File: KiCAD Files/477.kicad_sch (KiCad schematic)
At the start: 28 parts, among them J1 USB_A, U1 STM32H7A3RGTx, U2 LM1117DT-3.3, U3 AT25SF081-SSHD-X, U4 AT25SF081-SSHD-X, U5 AT25SF081-SSHD-X, U6 AT25SF081-SSHD-X, Y1 Crystal

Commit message: checking kicad files
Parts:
- C1: value C -> 10u; symbol Device:C -> CustomSymbols:C
- C2: value C -> 22u; symbol Device:C -> CustomSymbols:C
- C3, C4, C5: symbol Device:C -> CustomSymbols:C
- DS1: symbol Display_Character:WC1602A -> CustomSymbols:WC1602A
- J1: symbol Connector:USB_A -> CustomSymbols:USB_A
- R1, R11, R12, R2, R3, R4, R5, R6, R7, R8, R9: symbol Device:R_US -> CustomSymbols:R_US
- R10: value R_US -> 1k; symbol Device:R_US -> CustomSymbols:R_US
- U1: symbol MCU_ST_STM32H7:STM32H7A3RGTx -> CustomSymbols:STM32H7A3RGTx
- U2: value LM1117DT-3.3 -> AZ1117IH-3.3TRG1; symbol Regulator_Linear:LM1117DT-3.3 -> CustomSymbols:LM1117DT-3.3
- U3, U4, U5, U6: value AT25SF081-SSHD-X -> MT29F4G01ABAFDWB-IT:F; symbol Memory_Flash:AT25SF081-SSHD-X -> CustomSymbols:AT25SF081-SSHD-X
- Y1: symbol Device:Crystal -> CustomSymbols:Crystal
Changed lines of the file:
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@@
 	)
 	(symbol
-		(lib_id "power:GND")
+		(lib_id "CustomSymbols:GND")
 		(at 142.24 87.63 0)
 		(unit 1)
@@
 	)
 	(symbol
-		(lib_id "Device:C")
+		(lib_id "CustomSymbols:C")
 		(at 142.24 83.82 0)
 		(unit 1)
@@
 	)
 	(symbol
-		(lib_id "Device:C")
+		(lib_id "CustomSymbols:C")
 		(at 140.97 34.29 0)
 		(unit 1)
@@
 			)
 		)
-		(property "Value" "C"
+		(property "Value" "10u"
 			(at 144.78 35.5599 0)
 			(effects
@@
 	)
 	(symbol
-		(lib_id "Device:C")
+		(lib_id "CustomSymbols:C")
 		(at 172.72 34.29 0)
 		(unit 1)
@@
 			)
 		)
-		(property "Value" "C"
+		(property "Value" "22u"
 			(at 176.53 35.5599 0)
 			(effects
@@
 	)
 	(symbol
-		(lib_id "Device:R_US")
+		(lib_id "CustomSymbols:R_US")
 		(at 207.01 82.55 0)
 		(unit 1)
@@
 	)
 	(symbol
-		(lib_id "power:GND")
+		(lib_id "CustomSymbols:GND")
 		(at 146.05 132.08 0)
 		(unit 1)
@@
 	)
 	(symbol
-		(lib_id "Memory_Flash:AT25SF081-SSHD-X")
+		(lib_id "CustomSymbols:AT25SF081-SSHD-X")
 		(at 212.09 119.38 0)
 		(unit 1)
@@
 			)
 		)
-		(property "Value" "AT25SF081-SSHD-X"
-			(at 189.738 132.08 0)
+		(property "Value" "MT29F4G01ABAFDWB-IT:F"
+			(at 185.42 132.842 0)
 			(effects
 				(font
@@
 	)
 	(symbol
-		(lib_id "power:+3.3V")
+		(lib_id "CustomSymbols:+3.3V")
 		(at 39.37 149.86 0)
 		(unit 1)
@@
 	)
 	(symbol
-		(lib_id "power:GND")
+		(lib_id "CustomSymbols:GND")
 		(at 54.61 121.92 0)
 		(unit 1)
@@
 	)
 	(symbol
-		(lib_id "power:GND")
+		(lib_id "CustomSymbols:GND")
 		(at 250.19 82.55 0)
 		(unit 1)
@@
 	)
 	(symbol
-		(lib_id "Device:R_US")
+		(lib_id "CustomSymbols:R_US")
 		(at 149.86 83.82 0)
 		(unit 1)
@@
 	)
 	(symbol
-		(lib_id "Display_Character:WC1602A")
+		(lib_id "CustomSymbols:WC1602A")
 		(at 39.37 170.18 0)
 		(unit 1)
@@
 	)
 	(symbol
-		(lib_id "Device:R_US")
+		(lib_id "CustomSymbols:R_US")
 		(at 201.93 82.55 0)
 		(unit 1)
@@
 	)
 	(symbol
-		(lib_id "Regulator_Linear:LM1117DT-3.3")
+		(lib_id "CustomSymbols:LM1117DT-3.3")
 		(at 156.21 30.48 0)
 		(unit 1)
@@
 			)
 		)
-		(property "Value" "LM1117DT-3.3"
+		(property "Value" "AZ1117IH-3.3TRG1"
 			(at 156.21 26.67 0)
 			(effects
@@
 	)
 	(symbol
-		(lib_id "Device:Crystal")
+		(lib_id "CustomSymbols:Crystal")
 		(at 209.55 27.94 90)
 		(unit 1)
@@
 	)
 	(symbol
-		(lib_id "Device:R_US")
+		(lib_id "CustomSymbols:R_US")
 		(at 58.42 151.13 0)
 		(unit 1)
@@
 	)
 	(symbol
-		(lib_id "power:+3.3V")
+		(lib_id "CustomSymbols:+3.3V")
 		(at 146.05 106.68 0)
 		(unit 1)
@@
 	)
 	(symbol
-		(lib_id "Device:R_US")
+		(lib_id "CustomSymbols:R_US")
 		(at 58.42 158.75 0)
 		(unit 1)
@@
 	)
 	(symbol
-		(lib_id "MCU_ST_STM32H7:STM32H7A3RGTx")
+		(lib_id "CustomSymbols:STM32H7A3RGTx")
 		(at 54.61 76.2 0)
 		(unit 1)
@@
 	)
 	(symbol
-		(lib_id "power:GND")
+		(lib_id "CustomSymbols:GND")
 		(at 180.34 132.08 0)
 		(unit 1)
@@
 	)
 	(symbol
-		(lib_id "Memory_Flash:AT25SF081-SSHD-X")
+		(lib_id "CustomSymbols:AT25SF081-SSHD-X")
 		(at 243.84 119.38 0)
 		(unit 1)
@@
 			)
 		)
-		(property "Value" "AT25SF081-SSHD-X"
-			(at 221.488 132.08 0)
+		(property "Value" "MT29F4G01ABAFDWB-IT:F"
+			(at 216.408 132.08 0)
 			(effects
 				(font
@@
 	)
 	(symbol
-		(lib_id "Device:R_US")
+		(lib_id "CustomSymbols:R_US")
 		(at 209.55 82.55 0)
 		(unit 1)
@@
 	)
 	(symbol
-		(lib_id "power:+3.3V")
+		(lib_id "CustomSymbols:+3.3V")
 		(at 58.42 147.32 0)
 		(unit 1)
@@
 	)
 	(symbol
-		(lib_id "Device:R_US")
+		(lib_id "CustomSymbols:R_US")
 		(at 214.63 82.55 0)
 		(unit 1)
@@
 	)
 	(symbol
-		(lib_id "power:GND")
+		(lib_id "CustomSymbols:GND")
 		(at 199.39 41.91 0)
 		(unit 1)
@@
 	)
 	(symbol
-		(lib_id "power:GND")
+		(lib_id "CustomSymbols:GND")
 		(at 160.02 80.01 0)
 		(unit 1)
@@
 	)
 	(symbol
-		(lib_id "power:GND")
+		(lib_id "CustomSymbols:GND")
 		(at 243.84 132.08 0)
 		(unit 1)
@@
 	)
 	(symbol
-		(lib_id "Device:R_US")
+		(lib_id "CustomSymbols:R_US")
 		(at 204.47 82.55 0)
 		(unit 1)
@@
 	)
 	(symbol
-		(lib_id "power:+3.3V")
+		(lib_id "CustomSymbols:+3.3V")
 		(at 243.84 106.68 0)
 		(unit 1)
@@
 	)
 	(symbol
-		(lib_id "Connector:USB_A")
+		(lib_id "CustomSymbols:USB_A")
 		(at 160.02 69.85 0)
 		(unit 1)
@@
 	)
 	(symbol
-		(lib_id "Device:R_US")
+		(lib_id "CustomSymbols:R_US")
 		(at 224.79 22.86 90)
 		(unit 1)
@@
 	)
 	(symbol
-		(lib_id "power:+3.3V")
+		(lib_id "CustomSymbols:+3.3V")
 		(at 250.19 66.04 0)
 		(unit 1)
@@
 	)
 	(symbol
-		(lib_id "Device:R_US")
+		(lib_id "CustomSymbols:R_US")
 		(at 217.17 82.55 0)
 		(unit 1)
@@
 			)
 		)
-		(property "Value" "R_US"
+		(property "Value" "1k"
 			(at 219.71 83.8199 0)
 			(effects
@@
 	)
 	(symbol
-		(lib_id "Device:C")
+		(lib_id "CustomSymbols:C")
 		(at 199.39 27.94 0)
 		(unit 1)
@@
 	)
 	(symbol
-		(lib_id "power:+3.3V")
+		(lib_id "CustomSymbols:+3.3V")
 		(at 54.61 27.94 0)
 		(unit 1)
@@
 	)
 	(symbol
-		(lib_id "power:GND")
+		(lib_id "CustomSymbols:GND")
 		(at 39.37 190.5 0)
 		(unit 1)
@@
 	)
 	(symbol
-		(lib_id "Device:R_US")
+		(lib_id "CustomSymbols:R_US")
 		(at 212.09 82.55 0)
 		(unit 1)
@@
 	)
 	(symbol
-		(lib_id "Memory_Flash:AT25SF081-SSHD-X")
+		(lib_id "CustomSymbols:AT25SF081-SSHD-X")
 		(at 146.05 119.38 0)
 		(unit 1)
@@
 			)
 		)
-		(property "Value" "AT25SF081-SSHD-X"
-			(at 123.698 132.08 0)
+		(property "Value" "MT29F4G01ABAFDWB-IT:F"
+			(at 119.888 133.35 0)
 			(effects
 				(font
@@
 	)
 	(symbol
-		(lib_id "power:GND")
+		(lib_id "CustomSymbols:GND")
 		(at 58.42 162.56 0)
 		(unit 1)
@@
 	)
 	(symbol
-		(lib_id "Device:C")
+		(lib_id "CustomSymbols:C")
 		(at 209.55 38.1 0)
 		(unit 1)
@@
 	)
 	(symbol
-		(lib_id "Device:R_US")
+		(lib_id "CustomSymbols:R_US")
 		(at 224.79 34.29 90)
 		(unit 1)
@@
 	)
 	(symbol
-		(lib_id "power:GND")
+		(lib_id "CustomSymbols:GND")
 		(at 156.21 38.1 0)
 		(unit 1)
@@
 	)
 	(symbol
-		(lib_id "power:+3.3V")
+		(lib_id "CustomSymbols:+3.3V")
 		(at 212.09 106.68 0)
 		(unit 1)
@@
 	)
 	(symbol
-		(lib_id "power:GND")
+		(lib_id "CustomSymbols:GND")
 		(at 212.09 132.08 0)
 		(unit 1)
@@
 	)
 	(symbol
-		(lib_id "power:+3.3V")
+		(lib_id "CustomSymbols:+3.3V")
 		(at 180.34 106.68 0)
 		(unit 1)
@@
 	)
 	(symbol
-		(lib_id "power:+5V")
+		(lib_id "CustomSymbols:+5V")
 		(at 140.97 30.48 0)
 		(unit 1)
@@
 	)
 	(symbol
-		(lib_id "Memory_Flash:AT25SF081-SSHD-X")
+		(lib_id "CustomSymbols:AT25SF081-SSHD-X")
 		(at 180.34 119.38 0)
 		(unit 1)
@@
 			)
 		)
-		(property "Value" "AT25SF081-SSHD-X"
-			(at 157.988 132.08 0)
+		(property "Value" "MT29F4G01ABAFDWB-IT:F"
+			(at 152.908 132.842 0)
 			(effects
 				(font

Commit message: finished pcb draft
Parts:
- removed C1: 10u, symbol CustomSymbols:C
- removed C3: C, symbol CustomSymbols:C
- removed J1: USB_A, symbol CustomSymbols:USB_A
- removed R1: R_US, symbol CustomSymbols:R_US
- removed U2: AZ1117IH-3.3TRG1, Package_TO_SOT_SMD:TO-252-3_TabPin2, symbol CustomSymbols:LM1117DT-3.3
- removed U3, U4, U5, U6: MT29F4G01ABAFDWB-IT:F, Package_SO:SOIC-8_3.9x4.9mm_P1.27mm, symbol CustomSymbols:AT25SF081-SSHD-X
- removed Y1: Crystal, symbol CustomSymbols:Crystal
- added C6: 10u, Capacitor_SMD:C_0805_2012Metric_Pad1.18x1.45mm_HandSolder, symbol CustomSymbols:C
- added IC1, IC2, IC3, IC4: W25N01GVSFIG, SOIC127P1032X264-16N, symbol CustomSymbols:W25N01GVSFIG
- added IC5: AZ1117IH-3.3TRG1, SOT230P700X180-4N, symbol CustomSymbols:AZ1117IH-3.3TRG1
- added J2: 6364372-2, 63643722, symbol CustomSymbols:6364372-2
- added Y2: ABM8G-48.000MHZ-18-D2Y-T, ABM8G, symbol CustomSymbols:ABM8G-48.000MHZ-18-D2Y-T
- C2, C4, C5: footprint (none) -> Capacitor_SMD:C_0805_2012Metric_Pad1.18x1.45mm_HandSolder
- R11, R12, R2, R3: footprint (none) -> Resistor_SMD:R_0805_2012Metric_Pad1.20x1.40mm_HandSolder
- R4, R5, R6, R7, R8, R9: value R_US -> 1k; footprint (none) -> Resistor_SMD:R_0805_2012Metric_Pad1.20x1.40mm_HandSolder
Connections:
- net 3.3V Source is gone; now on net +3.3V: C2.1
- net PB0 is gone; now on net PB0/KeyR1: R4.2
- net PB1 is gone; now on net PB1/KeyR2: R5.2
- net PB10 is gone; now on net PB10/LCD SCK: DS1.12 (D5)
- net PB12 is gone; now on net PB12/LCD NSS: DS1.16 (LED(-))
- net PB2 is gone; now on net PB2/KeyR3: R6.2
- net PB3 is gone; now on net PB3/KeyR4: R7.2
- net PB4 is gone; now on net PB4/KeyC1: R8.2
- net PB5 is gone; now on net PB5/KeyC2: R9.2
- net PC1 is gone; now on net PC1/LCD MOSI: DS1.14 (D7)
- net PC14 is gone; now on an unnamed net: R2.2
- net PC15 is gone; now on net PC15/OSC OUT: R3.2
- net +3.3V: now also IC1.2 (VCC), IC2.2 (VCC), IC3.2 (VCC), IC4.2 (VCC), IC5.2 (OUTPUT)
- net +5V: now also C6.1, IC5.3 (INPUT), J2.1
- net GND: now also C6.2, IC1.10 (GND), IC1.11 (NC_5), IC1.12 (NC_6), IC1.13 (NC_7), IC1.14 (NC_8), IC1.3 (NC_1), IC1.4 (NC_2), IC1.5 (NC_3), IC1.6 (NC_4), IC2.10 (GND), IC2.11 (NC_5), IC2.12 (NC_6), IC2.13 (NC_7), IC2.14 (NC_8), IC2.3 (NC_1), IC2.4 (NC_2), IC2.5 (NC_3), IC2.6 (NC_4), IC3.10 (GND), IC3.11 (NC_5), IC3.12 (NC_6), IC3.13 (NC_7), IC3.14 (NC_8), IC3.3 (NC_1), IC3.4 (NC_2), IC3.5 (NC_3), IC3.6 (NC_4), IC4.10 (GND), IC4.11 (NC_5), IC4.12 (NC_6), IC4.13 (NC_7), IC4.14 (NC_8), IC4.3 (NC_1), IC4.4 (NC_2), IC4.5 (NC_3), IC4.6 (NC_4), IC5.1 (ADJ/GND), J2.4, J2.MH1, J2.MH2, Y2.2 (GND_1), Y2.4 (GND_2)
- net at C4.1, R3.1: now also Y2.3 (XTAL_2)
- net at C5.1: now also Y2.1 (XTAL_1); no longer R2.1
- net CS1 renamed PA0/CS1
- net PA0/CS1: now also IC1.7 (/CS)
- net CS2 renamed PA1/CS2
- net PA1/CS2: now also IC2.7 (/CS)
- net CS3 renamed PA2/CS3
- net PA2/CS3: now also IC3.7 (/CS)
- net CS4 renamed PA3/CS4
- net PA3/CS4: now also IC4.7 (/CS)
- net Flash MISO renamed PA6/MISO
- net PA6/MISO: now also IC1.8 (DO_(IO1_)), IC2.8 (DO_(IO1_)), IC3.8 (DO_(IO1_)), IC4.8 (DO_(IO1_))
- net Flash MOSI renamed PA7/MOSI
- net PA7/MOSI: now also IC1.15 (DI_(IO0_)), IC2.15 (DI_(IO0_)), IC3.15 (DI_(IO0_)), IC4.15 (DI_(IO0_))
- net Flash SCK renamed PA5/SCK
- net PA5/SCK: now also IC1.16 (CLK), IC2.16 (CLK), IC3.16 (CLK), IC4.16 (CLK)
- net KeypadC1 renamed PB4/KeyC1
- net KeypadC2 renamed PB5/KeyC2
- net KeypadC3 renamed PB6/KeyC3
- net KeypadR1 renamed PB0/KeyR1
- net KeypadR2 renamed PB1/KeyR2
- net KeypadR3 renamed PB2/KeyR3
- net KeypadR4 renamed PB3/KeyR4
- net LCD MOSI renamed PC1/LCD MOSI
- net LCD NSS renamed PB12/LCD NSS
- net LCD SCK renamed PB10/LCD SCK
- net OSC IN renamed PC14/OSC IN
- net PC14/OSC IN: now also R2.1
- net OSC OUT renamed PC15/OSC OUT
- net PB6 renamed PB5/KeyC3
- net USB+ renamed PA12/USB+
- net PA12/USB+: now also J2.3
- net USB- renamed PA11/USB-
- net PA11/USB-: now also J2.2
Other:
- moved on the sheet: C4, C5, R10, R2, R3, U7

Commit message: tweaked schematic
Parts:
- removed R2: R_US, Resistor_SMD:R_0805_2012Metric_Pad1.20x1.40mm_HandSolder, symbol CustomSymbols:R_US
- added C1: 2.2n, Capacitor_SMD:C_0805_2012Metric_Pad1.18x1.45mm_HandSolder, symbol CustomSymbols:C
- added R1: 1M, Resistor_SMD:R_0805_2012Metric_Pad1.20x1.40mm_HandSolder, symbol CustomSymbols:R_US
- C4, C5: value C -> 10p
- R3: value R_US -> 330
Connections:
- net GND: now also C1.2, R1.2; no longer J2.MH1, J2.MH2
- net PC14/OSC IN: now also C5.1, Y2.1 (XTAL_1)
- net PC6/HOLD1: now reaches IC1.1 (/HOLD_(IO3))
- net PC6/HOLD1: now also U1.37 (PC6)
- net PC2/WP1: now reaches IC1.9 (/WP_(IO2_))
- net PC2/WP1: now also U1.10 (PC2)
- net PC9/HOLD3: now reaches IC3.1 (/HOLD_(IO3))
- net PC9/HOLD3: now also U1.39 (PC9)
- net PC4/WP3: now reaches IC3.9 (/WP_(IO2_))
- net PC4/WP3: now also U1.24 (PC4)
- net PC3/WP2: now reaches U1.11 (PC3)
- net PC3/WP2: now also IC2.9 (/WP_(IO2_))
- net PC5/WP4: now reaches U1.25 (PC5)
- net PC5/WP4: now also IC4.9 (/WP_(IO2_))
- net PC7/HOLD2: now reaches U1.38 (PC7)
- net PC7/HOLD2: now also IC2.1 (/HOLD_(IO3))
- net PC10/HOLD4: now reaches U1.51 (PC10)
- net PC10/HOLD4: now also IC4.1 (/HOLD_(IO3))
- net GPIO TBD: now reaches U8.5 (WKUP)
- new net: C1.1, J2.MH2, R1.1
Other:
- moved on the sheet: U8

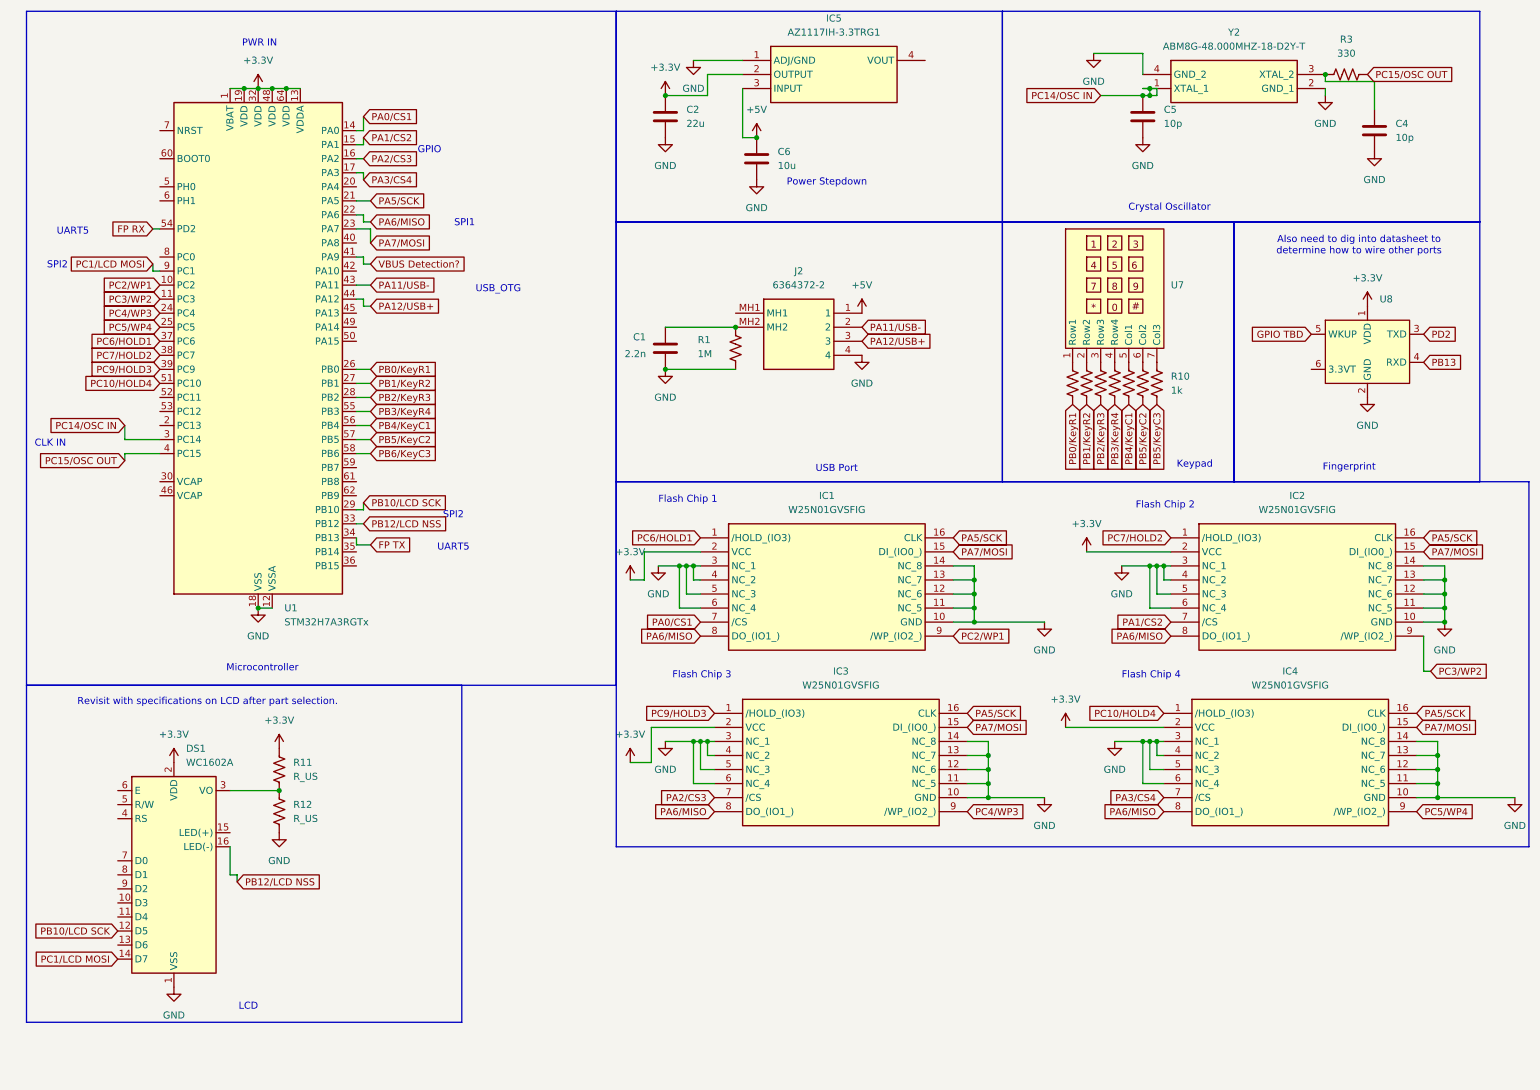
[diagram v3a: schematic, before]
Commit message: tweaked diagram and pin out setup.
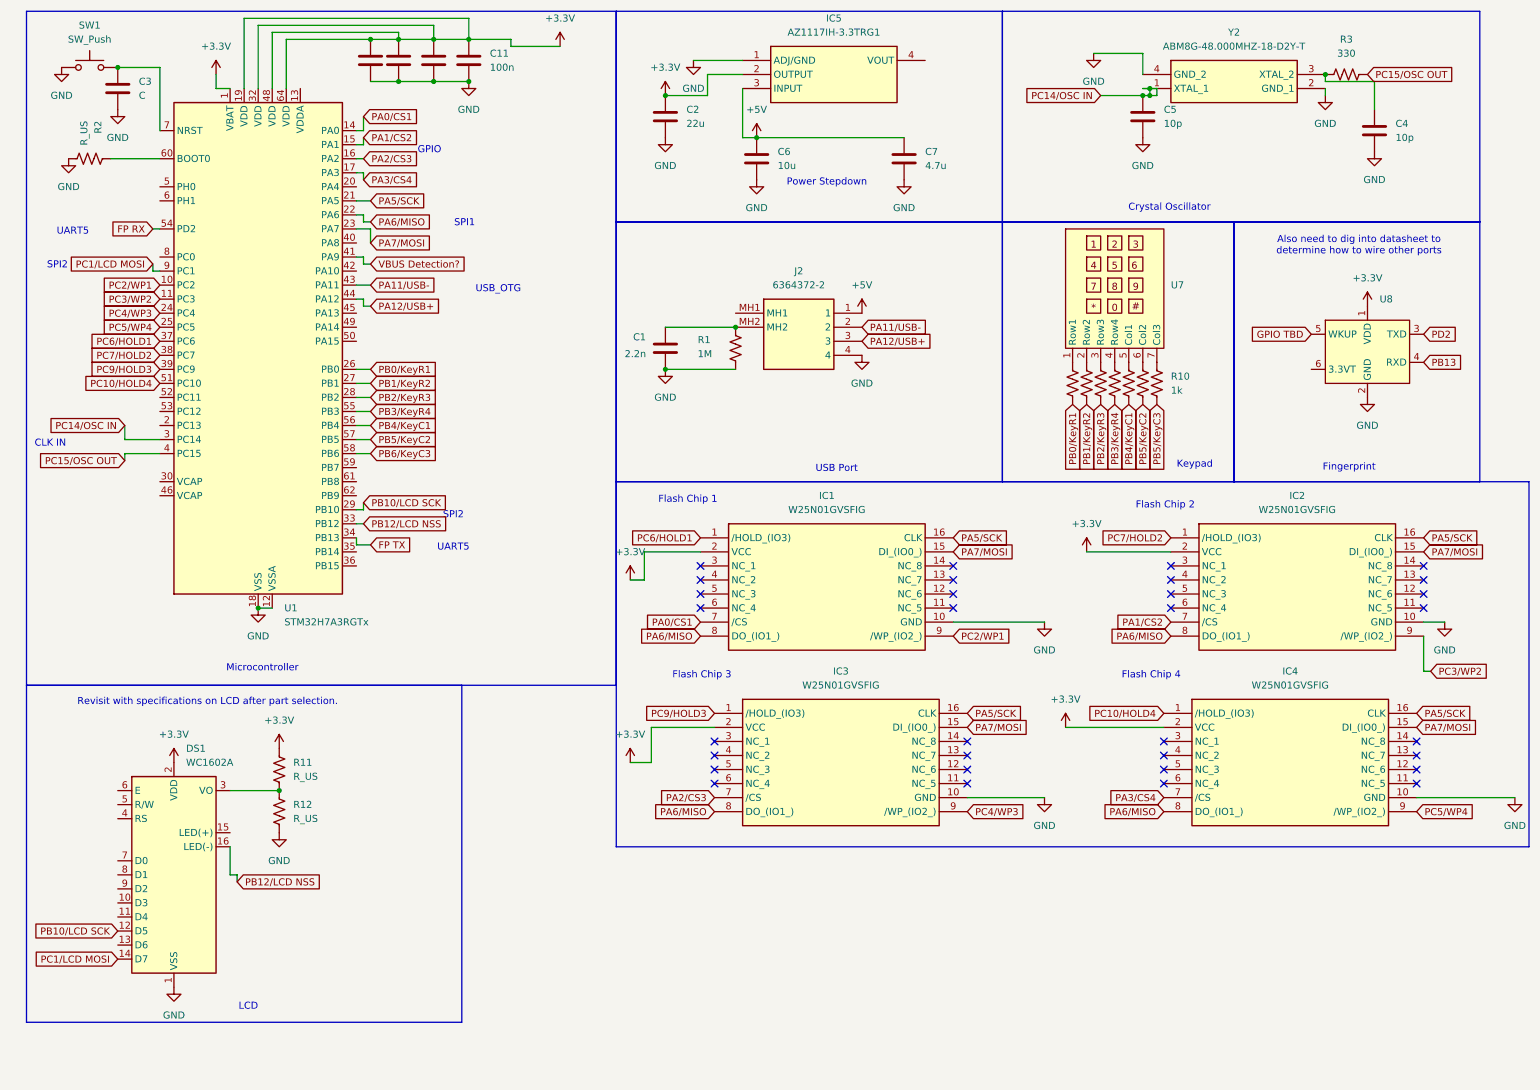
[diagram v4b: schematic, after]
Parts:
- added C10, C11, C8, C9: 100n, Capacitor_SMD:C_0805_2012Metric_Pad1.18x1.45mm_HandSolder, symbol CustomSymbols:C
- added C3: C, Capacitor_SMD:C_0805_2012Metric_Pad1.18x1.45mm_HandSolder, symbol CustomSymbols:C
- added C7: 4.7u, Capacitor_SMD:C_0805_2012Metric_Pad1.18x1.45mm_HandSolder, symbol CustomSymbols:C
- added R2: R_US, Resistor_SMD:R_0805_2012Metric_Pad1.20x1.40mm_HandSolder, symbol CustomSymbols:R_US
- added SW1: SW_Push, symbol Switch:SW_Push
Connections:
- net +3.3V: now also C10.1, C11.1, C8.1, C9.1; no longer U1.13 (VDDA)
- net +5V: now also C7.1
- net GND: now also C10.2, C11.2, C3.2, C7.2, C8.2, C9.2, R2.2, SW1.1; no longer IC1.11 (NC_5), IC1.12 (NC_6), IC1.13 (NC_7), IC1.14 (NC_8), IC1.3 (NC_1), IC1.4 (NC_2), IC1.5 (NC_3), IC1.6 (NC_4), IC2.11 (NC_5), IC2.12 (NC_6), IC2.13 (NC_7), IC2.14 (NC_8), IC2.3 (NC_1), IC2.4 (NC_2), IC2.5 (NC_3), IC2.6 (NC_4), IC3.11 (NC_5), IC3.12 (NC_6), IC3.13 (NC_7), IC3.14 (NC_8), IC3.3 (NC_1), IC3.4 (NC_2), IC3.5 (NC_3), IC3.6 (NC_4), IC4.11 (NC_5), IC4.12 (NC_6), IC4.13 (NC_7), IC4.14 (NC_8), IC4.3 (NC_1), IC4.4 (NC_2), IC4.5 (NC_3), IC4.6 (NC_4)
- net at U1.60 (BOOT0): now also R2.1
- net at U1.7 (NRST): now also C3.1, SW1.2
- no-connect marks 0 -> 32
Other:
- note removed: "PWR IN"

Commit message: updated schematic
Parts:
- removed U8: ~, symbol CustomSymbols:fingerprint_sensor
- added C12: 2.2n, Capacitor_SMD:C_0805_2012Metric_Pad1.18x1.45mm_HandSolder, symbol CustomSymbols:C
- added J1: BM06B-SRSS-TBT_LF__SN_, BM06BSRSSTBTLFSN, symbol CustomSymbols:BM06B-SRSS-TBT_LF__SN_
- added R13: 1M, Resistor_SMD:R_0805_2012Metric_Pad1.20x1.40mm_HandSolder, symbol CustomSymbols:R_US
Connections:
- net +3.3V: now also C7.1, IC5.4 (VOUT), J1.1, J1.5, J1.6
- net +5V: no longer C7.1
- net GND: now also C12.2, J1.2, R13.2
- net FP TX renamed PB13/FP TX
- net PB13/FP TX: now also J1.4
- new net: C12.1, J1.MP2, R13.1
- new net PD2/FP RX: J1.3
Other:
- note removed: "Also need to dig into datasheet to determine how to wire other ports"
